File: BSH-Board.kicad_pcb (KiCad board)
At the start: 2 copper layers, 24 x 38 mm, 73 parts, among them J1 667101210103, J2 MICRO QTZB5.0, Q1 MMST3904, SW1 TS-3025-B-C-B, SW2 TS-3025-B-C-B, SW3 SW_DIP_x01, U1 74LVC1G07, U2 74LVC1G17, U3 AP63203WU, U4 ESP32-C6-MINI-1-N4

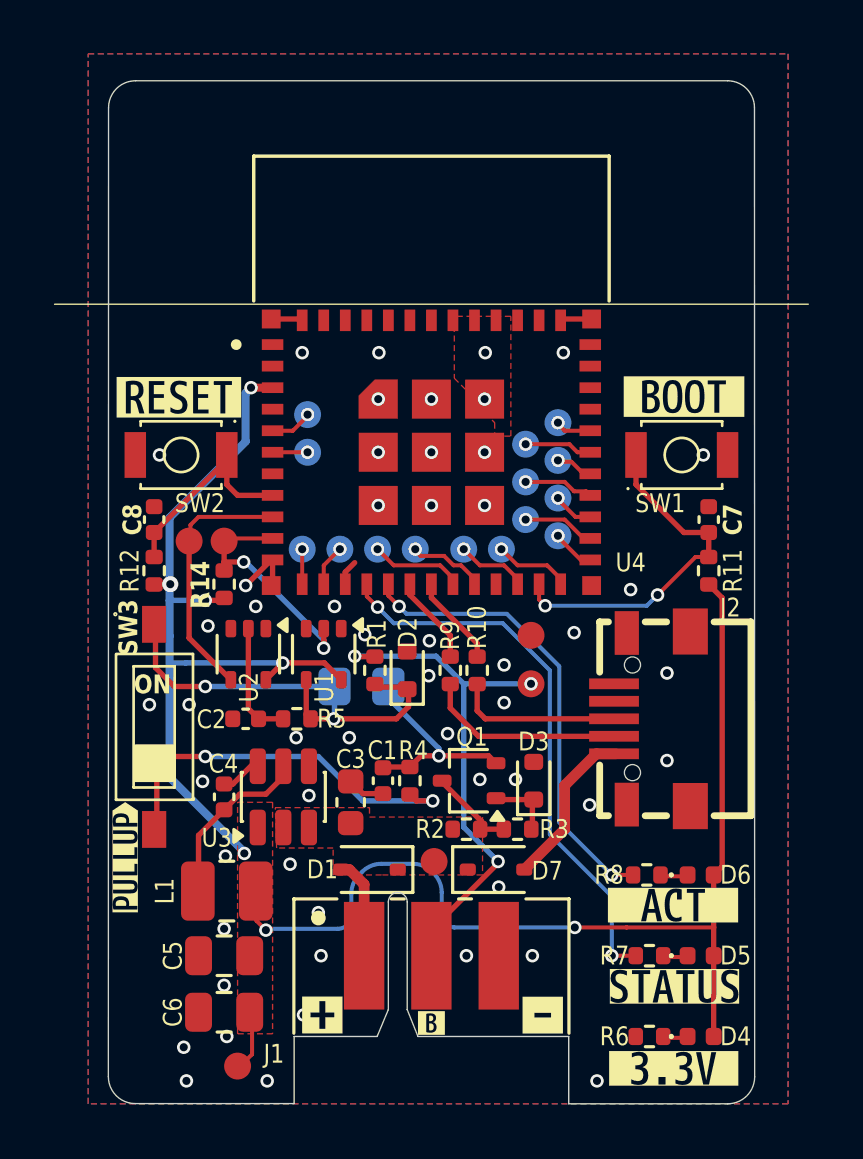
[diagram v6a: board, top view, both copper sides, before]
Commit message: Replaced V-Cuts with Mousebites
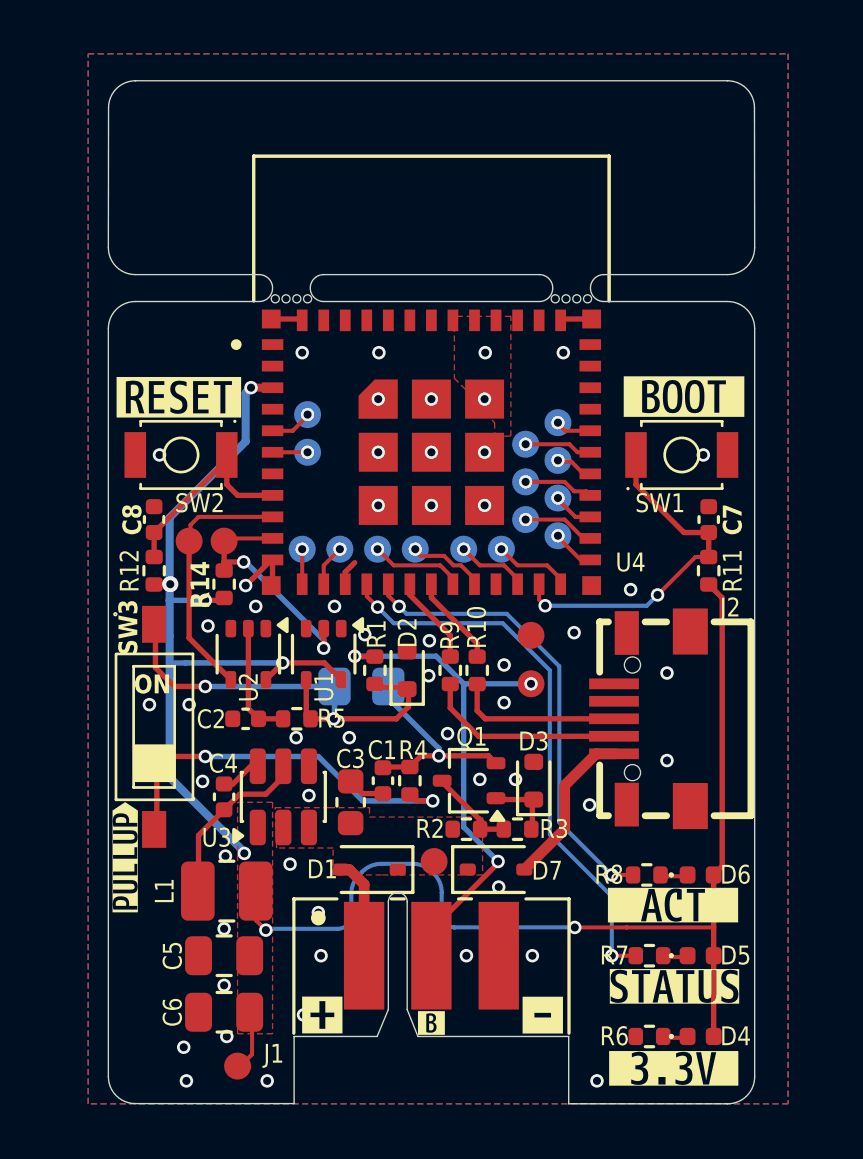
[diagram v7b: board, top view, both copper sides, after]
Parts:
- added REF**: Mousbite, Mousebites:Mousbite, F.Cu at (127.2, 61.1)
- added REF**: Mousbite, Mousebites:Mousbite, F.Cu at (116.8, 61.1)
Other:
- outline, holes or cut-outs redrawn
